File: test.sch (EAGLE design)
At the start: 17 parts

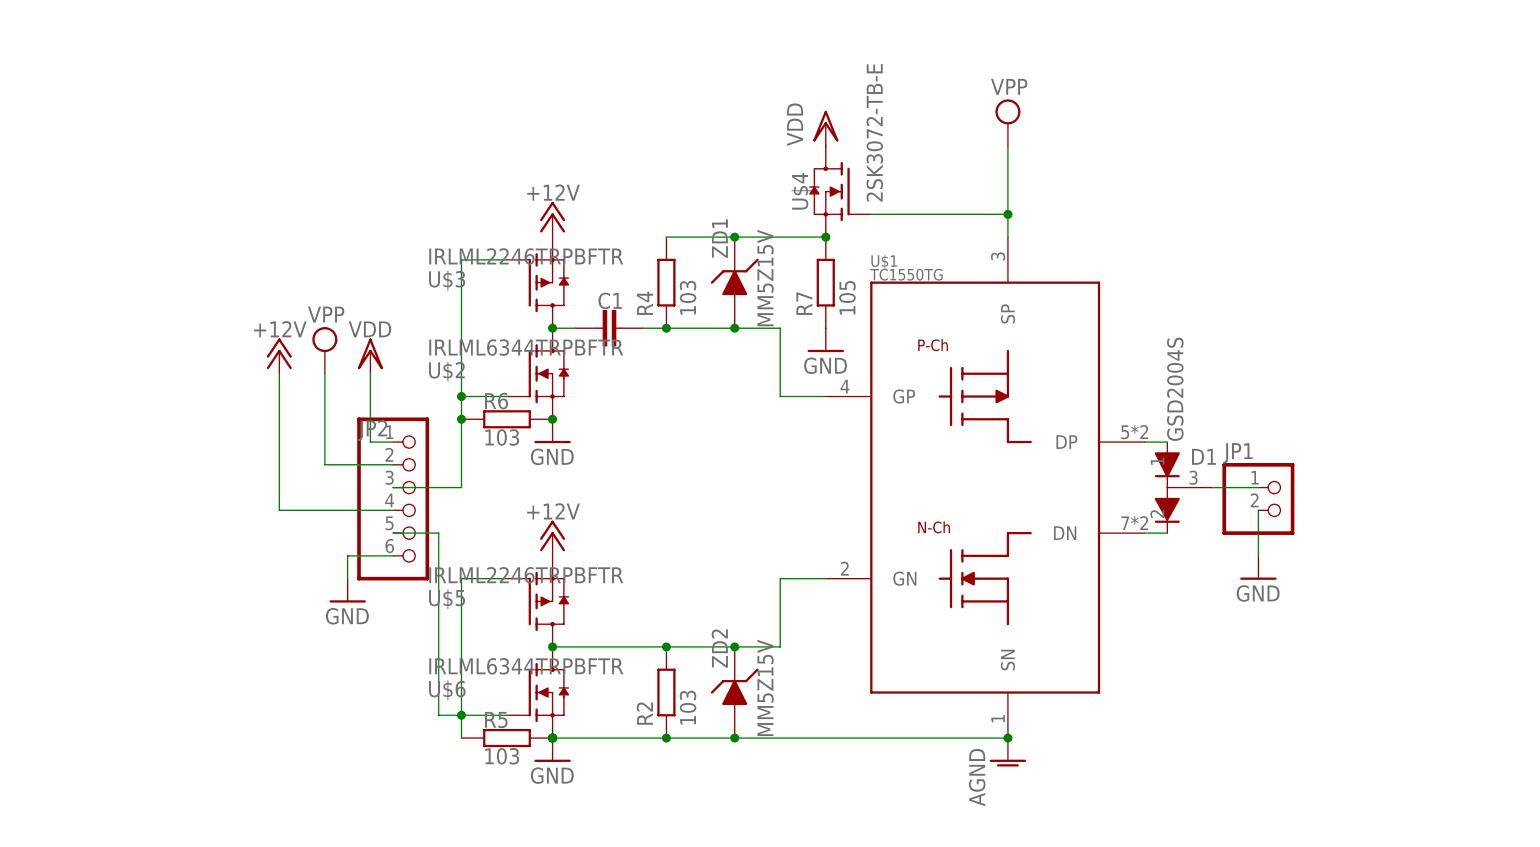
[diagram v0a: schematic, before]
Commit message: added cmos designed fet driver
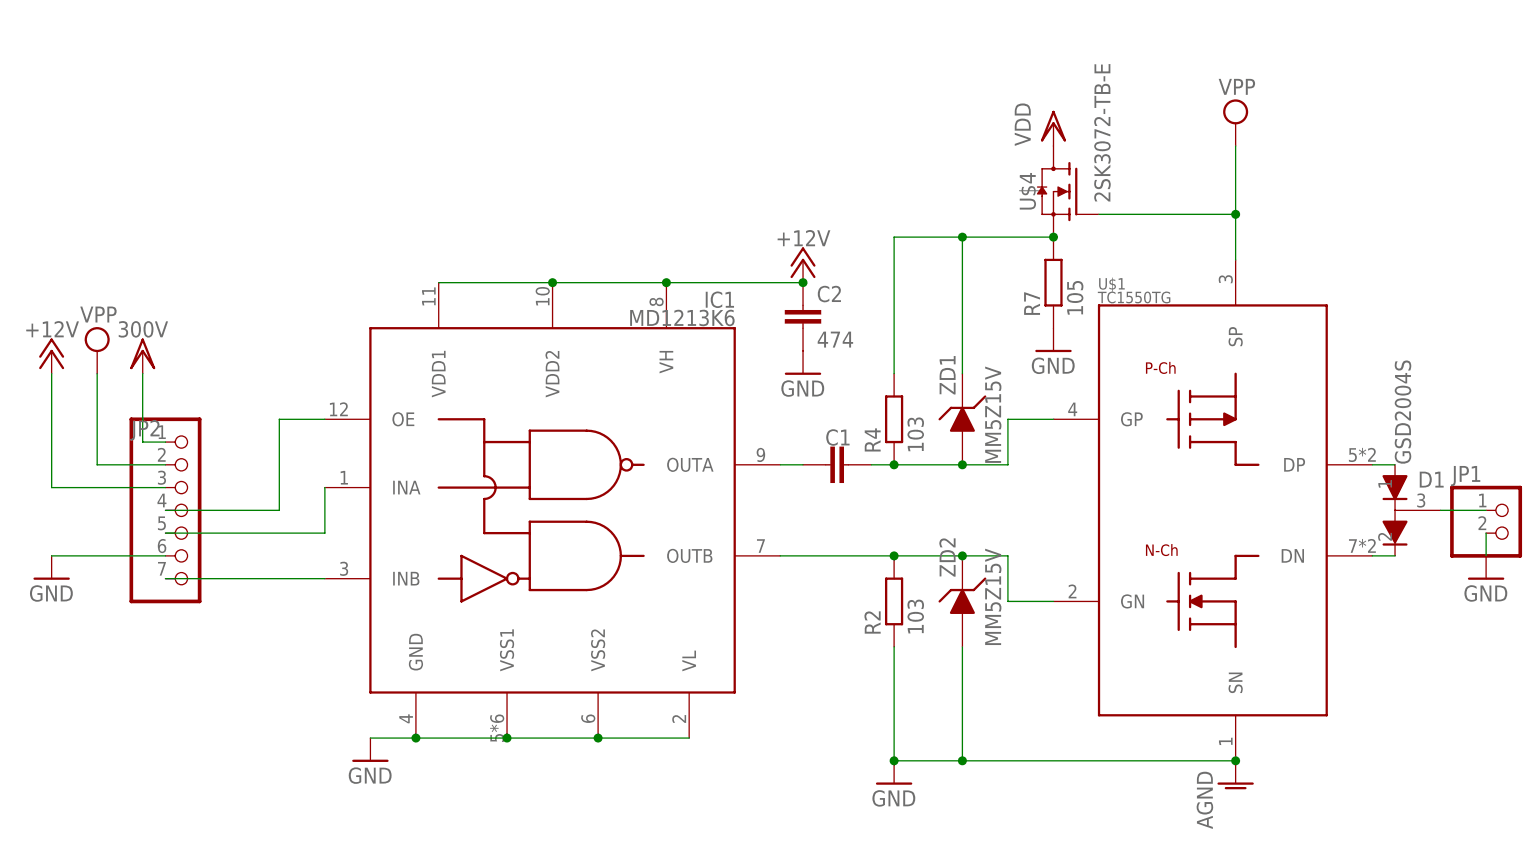
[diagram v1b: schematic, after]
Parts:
- removed R5, R6: 103, rcl:R-EU_0204/5
- removed U$2, U$6: IRLML6344TRPBFTR, Transistor-FET:IRLML6344TRPBFTR
- removed U$3, U$5: IRLML2246TRPBFTR, Transistor-FET:IRLML2246TRPBFTR
- added C2: 474, rcl:C-EU025-024X044
- added IC1: MD1213K6, md1213:MD1213K6
- JP2: device pinhead:PINHD-1X6 -> pinhead:PINHD-1X7
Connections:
- new net N$10: IC1.INB, JP2.7
- net +12V: now also C2.1, IC1.VDD1, IC1.VDD2, IC1.VH, JP2.3; no longer JP2.4, U$3.S, U$5.S
- net GND: now also C2.2, IC1.GND, IC1.VL, IC1.VSS1, IC1.VSS2; no longer R5.1, R6.1, U$2.S, U$6.S
- net N$1: now also IC1.OUTB; no longer U$5.D, U$6.D
- net N$2: now also IC1.OUTA; no longer U$2.D, U$3.D
- net N$4: now also IC1.INA; no longer R5.2, U$5.G, U$6.G
- net N$5: now also IC1.OE, JP2.4; no longer JP2.3, R6.2, U$2.G, U$3.G
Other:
- moved on the sheet: C1, D1, JP1, R2, R4, R7, U$1, U$4, ZD1, ZD2

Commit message: modified a value of 300V source symbol; Having a ploblem probably caused by Capacitor which require 240ms to charge
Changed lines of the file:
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@@
 <part name="D1" library="Diode_Vishay" library_urn="urn:adsk.eagle:library:10199852" deviceset="GSD2004S" device="" package3d_urn="urn:adsk.eagle:package:10199855/1"/>
 <part name="P+2" library="supply1" library_urn="urn:adsk.eagle:library:371" deviceset="+12V" device=""/>
-<part name="VDD1" library="supply1" library_urn="urn:adsk.eagle:library:371" deviceset="VDD" device=""/>
+<part name="VDD1" library="supply1" library_urn="urn:adsk.eagle:library:371" deviceset="VDD" device="" value="300V"/>
 <part name="VDD2" library="supply1" library_urn="urn:adsk.eagle:library:371" deviceset="VDD" device="" value="300V"/>
 <part name="U$4" library="Transistor-FET" library_urn="urn:adsk.eagle:library:11887002" deviceset="2SK3072-TB-E" device="" package3d_urn="urn:adsk.eagle:package:11886978/1"/>
@@
 <part name="P+3" library="supply1" library_urn="urn:adsk.eagle:library:371" deviceset="+12V" device=""/>
 <part name="C1" library="rcl" library_urn="urn:adsk.eagle:library:334" deviceset="C-EU" device="C3216" package3d_urn="urn:adsk.eagle:package:23628/2"/>
-<part name="IC1" library="md1213" library_urn="urn:adsk.eagle:library:9976036" deviceset="MD1213K6" device="" package3d_urn="urn:adsk.eagle:package:9976039/5"/>
+<part name="IC1" library="md1213" library_urn="urn:adsk.eagle:library:9976036" deviceset="MD1213K6" device="" package3d_urn="urn:adsk.eagle:package:9976039/6"/>
 <part name="GND1" library="supply1" library_urn="urn:adsk.eagle:library:371" deviceset="GND" device=""/>
 <part name="GND2" library="supply1" library_urn="urn:adsk.eagle:library:371" deviceset="GND" device=""/>
